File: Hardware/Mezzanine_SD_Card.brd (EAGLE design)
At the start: 30.5 x 44.5 mm, 16 parts, among them U1 USD-SOCKETNEW, U2 EDISON_CONNECTOR_FULLMOUNTING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, U3 EDISON_CONNECTOR_FULLHEADER

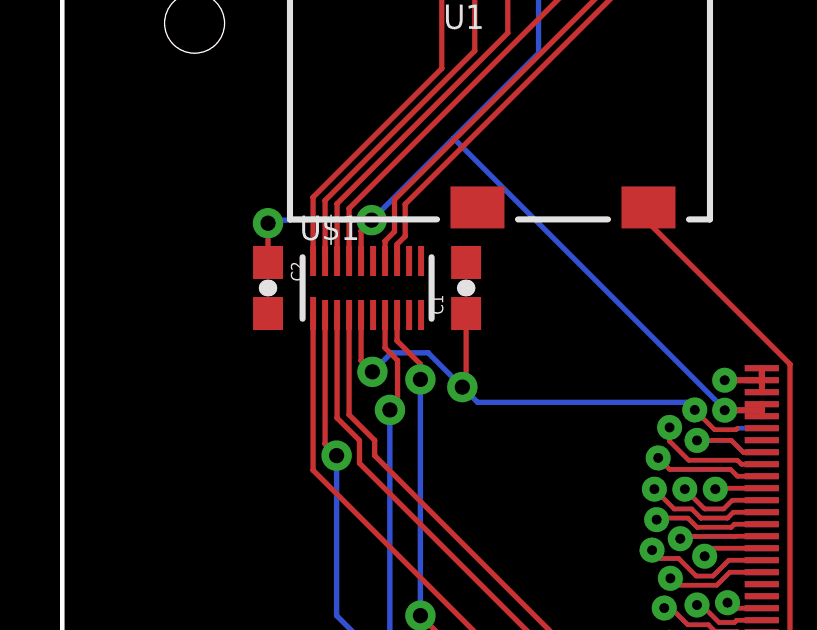
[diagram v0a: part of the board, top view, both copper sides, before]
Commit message: fixed OE to high
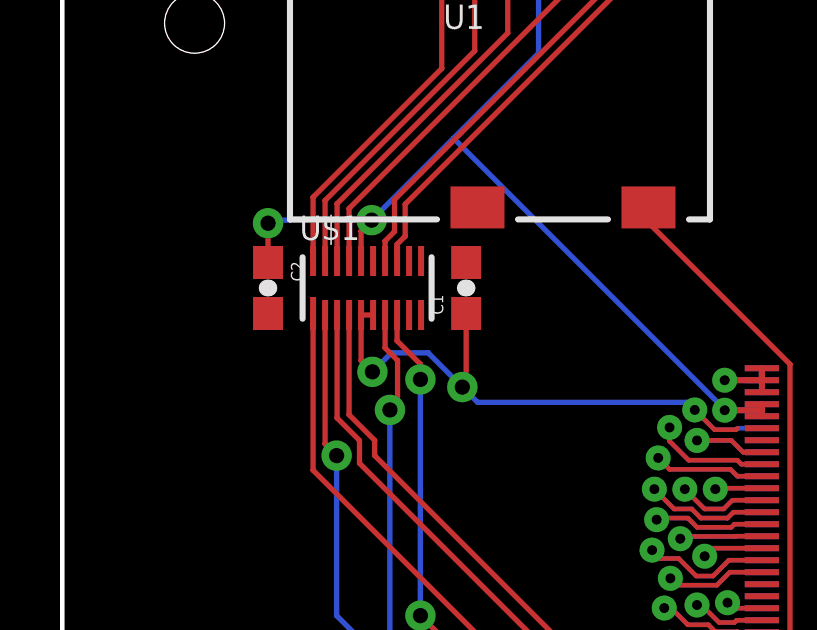
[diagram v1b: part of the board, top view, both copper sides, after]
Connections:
- net 1.8V: now also U$1.P$6
- net GND: no longer U$1.P$6
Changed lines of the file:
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@@
 <contactref element="U$1" pad="P$15"/>
 <contactref element="U1" pad="6"/>
-<contactref element="U$1" pad="P$6"/>
 <contactref element="C1" pad="2"/>
 <contactref element="C2" pad="2"/>
@@
 <wire x1="13.462" y1="24.804" x2="13.462" y2="22.479" width="0.1778" layer="1"/>
 <wire x1="13.462" y1="22.479" x2="13.335" y2="22.352" width="0.1778" layer="1"/>
+<contactref element="U$1" pad="P$6"/>
 <wire x1="23.32" y1="20.98" x2="23.32" y2="20.9798" width="0" layer="19" extent="1-16"/>
+<wire x1="9.96" y1="24.754" x2="10.36" y2="24.754" width="0.1778" layer="1"/>
 </signal>
 <signal name="FW_RCVR">

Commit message: work in progress
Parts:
- added SJ1, SJ2, SJ3: JUMPER-PAD-2-NO, SparkFun-Passives:PAD-JUMPER-2-NO_NO_SILK
- moved C1 2.54 mm to (13.5, 23.1)
- moved C2 2.54 mm to (6.86, 23.1)
- moved U$1 2.54 mm to (10.2, 23.1)
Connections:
- removed net N$4: U$1.P$17, U1.5
- new net SCK: SJ3.2, U$1.P$12, U$1.P$17, U1.5
- new net SCK_FB: SJ1.2, U$1.P$9
- net GP78_SD_0_CLK: now also SJ2.2
- net GP84_SD_CLK_FB: now also SJ1.1, SJ2.1, SJ3.1
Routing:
- net GP82_SD_0_DAT2: track 28.9 -> 7.36 mm
- net GP81_SD_0_DAT1: track 29.5 -> 8.75 mm, vias 3 -> 1
- net GP79_SD_0_CMD: track 27.4 -> 8.08 mm
- net GP78_SD_0_CLK: track 25.3 -> 6.88 mm
- net SCK: track 0.00 -> 17.7 mm
- net 1.8V: track 21.0 -> 5.73 mm, vias 3 -> 1
- net N$4: track 15.2 -> 0.00 mm
- net GP80_SD_0_DAT0: track 29.4 -> 17.9 mm, vias 2 -> 1
- net GP83_SD_0_DAT3: track 31.0 -> 20.9 mm, vias 2 -> 1
- net SCK_FB: track 0.00 -> 7.65 mm
- net GP84_SD_CLK_FB: track 4.87 -> 11.5 mm
- net 3.3V: track 36.1 -> 38.6 mm
- net N$5: track 15.6 -> 18.1 mm
- net N$6: track 15.9 -> 18.4 mm
- net N$3: track 14.4 -> 17.0 mm
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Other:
- board text added: "Micro SD Block"
- board text added: "Note: Units are in Inches"
- board text added: "v02"
- board text removed: "Connectors Go Here"
- board text removed: "LED's and selector switches go here"
- board text removed: "Max Board Length"
- board text removed: "Micro SD"
- board text removed: "Nothing goes here... I mean it."
- board text removed: "v01"

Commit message: work in progress
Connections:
- new net DCIN: U2.14, U3.14
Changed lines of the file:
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@@
 <wire x1="12.8778" y1="19.685" x2="17.457" y2="19.685" width="0.1524" layer="1"/>
+</signal>
+<signal name="DCIN">
+<contactref element="U2" pad="14"/>
+<contactref element="U3" pad="14"/>
+<wire x1="23.32" y1="20.5798" x2="23.32" y2="20.58" width="0" layer="19" extent="1-16"/>
 </signal>
 </signals>

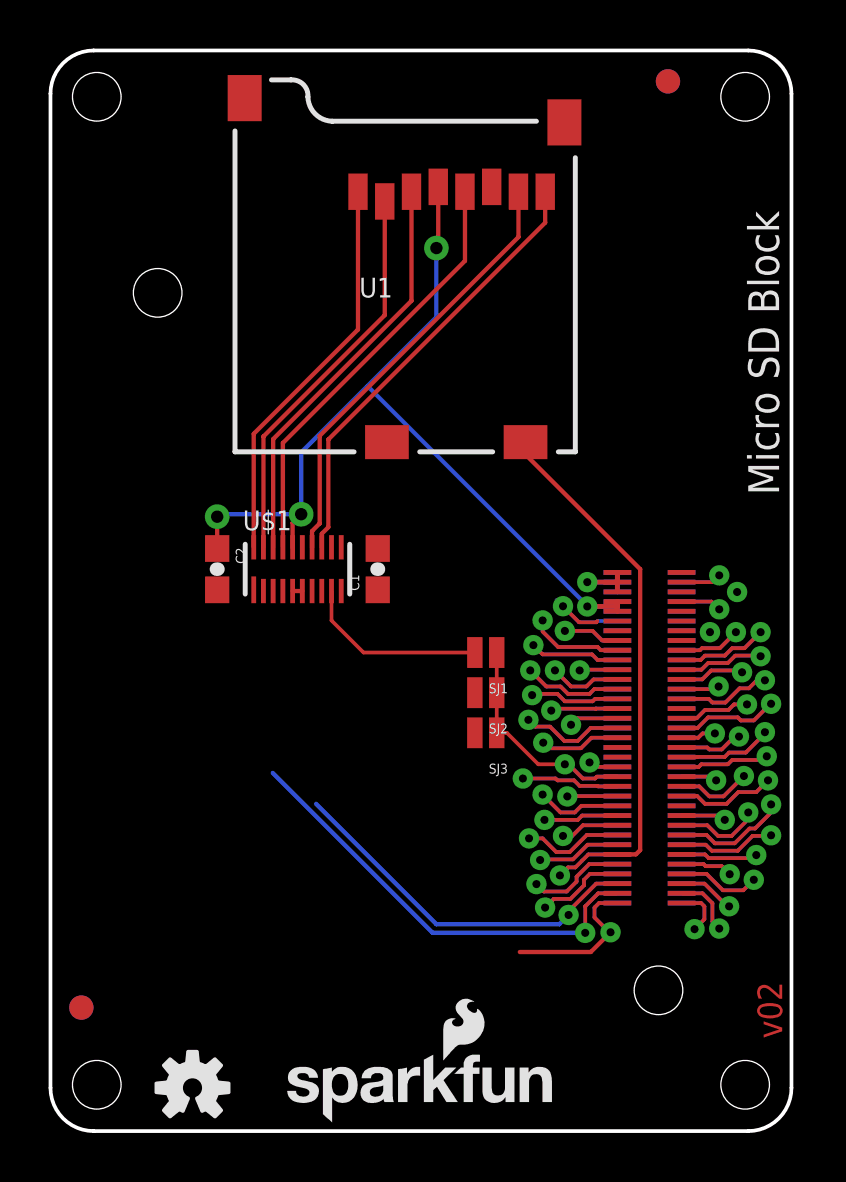
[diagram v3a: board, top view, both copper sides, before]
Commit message: Added DCIN pin cleaned up dimensions cleaned up names on board created clock feedback test circuit
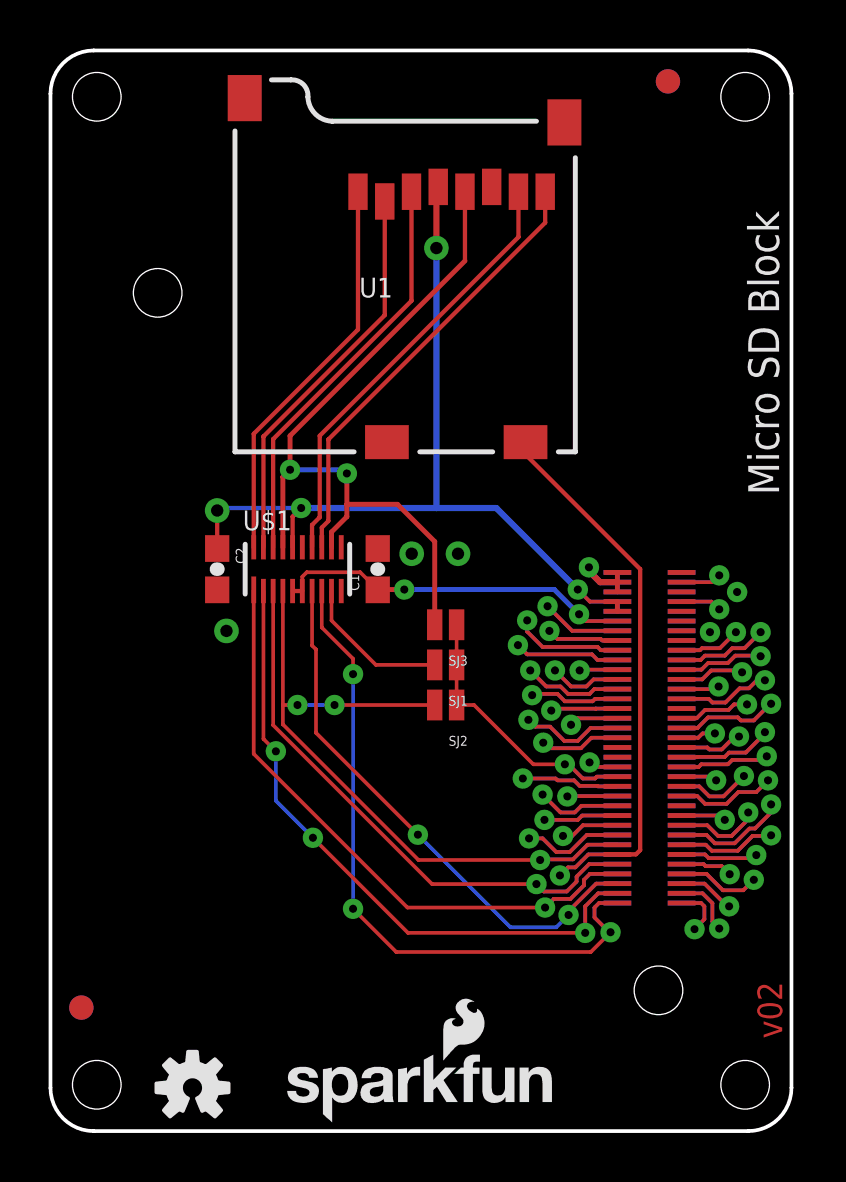
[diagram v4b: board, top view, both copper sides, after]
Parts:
- moved SJ3 4.74 mm to (16.3, 20.8)
- moved SJ1 1.73 mm to (16.3, 19.2)
- moved SJ2 1.73 mm to (16.3, 17.5)
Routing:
- net GP78_SD_0_CLK: track 6.88 -> 31.5 mm, vias 1 -> 3
- net GP82_SD_0_DAT2: track 7.36 -> 28.7 mm
- net GP81_SD_0_DAT1: track 8.75 -> 29.9 mm, vias 1 -> 3
- net GP79_SD_0_CMD: track 8.08 -> 27.1 mm
- net SCK: track 17.7 -> 31.1 mm, vias 0 -> 2
- net 1.8V: track 5.73 -> 16.6 mm, vias 1 -> 2
- net GP83_SD_0_DAT3: track 20.9 -> 29.1 mm, vias 1 -> 3
- net GP80_SD_0_DAT0: track 17.9 -> 25.1 mm, vias 1 -> 2
- net DCIN: track 0.00 -> 6.58 mm, vias 0 -> 1
- net GP84_SD_CLK_FB: track 11.5 -> 13.6 mm
- net SCK_FB: track 7.65 -> 6.21 mm
- net 3.3V: track 38.6 -> 37.3 mm
- net USB_VBUS: track 7.42 -> 8.69 mm
- net USB_DP: track 4.65 -> 5.92 mm
- net USB_DN: track 7.70 -> 8.97 mm
